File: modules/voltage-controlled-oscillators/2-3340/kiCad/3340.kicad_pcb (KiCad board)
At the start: 2 copper layers, 21 parts, among them J1 PWR, J2 INPUT, J3 OUTPUT

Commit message: cleaning up the main readme, update for 3340-vco
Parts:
- removed C1, C2: 47uF, Capacitor_THT:CP_Radial_D6.3mm_P2.50mm
- removed C3: 0.1uF, Capacitor_THT:CP_Radial_D4.0mm_P2.00mm
- removed the C5 at (108.2, 67.0)
- removed the C5 at (97.8, 71.2)
- removed the C6 at (94.7, 80.9)
- removed the C6 at (87.5, 80.5)
- added C10: 47uF, Capacitor_THT:CP_Radial_D6.3mm_P2.50mm, F.Cu at (34.4, 50.0)
- added C11: 0.1uF, Capacitor_THT:CP_Radial_D4.0mm_P2.00mm, F.Cu at (41.7, 42.1)
- added C12: 0.1uF, Capacitor_THT:CP_Radial_D4.0mm_P2.00mm, F.Cu at (41.7, 47.7)
- added C5: 0.1uF, Capacitor_THT:CP_Radial_D4.0mm_P2.00mm, F.Cu at (95.4, 94.5)
- added C6: 0.1uF, Capacitor_THT:CP_Radial_D4.0mm_P2.00mm, F.Cu at (95.4, 100.0)
- added C7: 0.1uF, Capacitor_THT:CP_Radial_D4.0mm_P2.00mm, F.Cu at (95.4, 105.5)
- added C9: 47uF, Capacitor_THT:CP_Radial_D6.3mm_P2.50mm, F.Cu at (34.4, 42.1)
- added J10: 1V/OCT, Synth:Jack_3.5mm_QingPu_WQP-PJ398SM_Vertical_CircularHoles, F.Cu at (226.2, 23.8)
- added J4: PWR, Synth:IDC-Header_2x08_P2.54mm_Vertical, B.Cu at (54.9, 65.3)
- added J5: SQR, Synth:Jack_3.5mm_QingPu_WQP-PJ398SM_Vertical_CircularHoles, F.Cu at (182.7, 23.9)
- added J6: TRI, Synth:Jack_3.5mm_QingPu_WQP-PJ398SM_Vertical_CircularHoles, F.Cu at (193.7, 23.9)
- added J7: SAW, Synth:Jack_3.5mm_QingPu_WQP-PJ398SM_Vertical_CircularHoles, F.Cu at (204.8, 23.9)
- added J8: SIN, Synth:Jack_3.5mm_QingPu_WQP-PJ398SM_Vertical_CircularHoles, F.Cu at (215.8, 23.9)
- added J9: PWM, Synth:Jack_3.5mm_QingPu_WQP-PJ398SM_Vertical_CircularHoles, F.Cu at (237.0, 23.6)
- added Q1: 2N3904, Package_TO_SOT_THT:TO-92L_HandSolder, F.Cu at (153.6, 77.2)
- added Q2: 2N3904, Package_TO_SOT_THT:TO-92L_HandSolder, F.Cu at (153.6, 83.3)
- added R10: 10M (OPT), Synth:R_Default (DIN0207), F.Cu at (116.5, 68.8)
- added R11: 100K, Synth:R_Default (DIN0207), F.Cu at (116.5, 72.9)
- added R12: 100K, Synth:R_Default (DIN0207), F.Cu at (116.5, 77.0)
- added R13: 100K, Synth:R_Default (DIN0207), F.Cu at (116.5, 81.0)
- added R14: 10K, 1%, Synth:R_Default (DIN0207), F.Cu at (116.5, 85.0)
- added R15: 10K, 1%, Synth:R_Default (DIN0207), F.Cu at (116.5, 89.1)
- added R16: 1K, Synth:R_Default (DIN0207), F.Cu at (116.5, 93.2)
- added R17: 1K, Synth:R_Default (DIN0207), F.Cu at (116.5, 97.2)
- added R18: 1K, Synth:R_Default (DIN0207), F.Cu at (116.5, 101.2)
- added R19: 1K, Synth:R_Default (DIN0207), F.Cu at (116.5, 105.3)
- added R20: 100K, Potentiometer_THT:Potentiometer_Bourns_3296W_Vertical, F.Cu at (159.7, 57.5)
- added R21: 2.2K, 1%, Synth:R_Default (DIN0207), F.Cu at (130.6, 58.2)
- added R22: 10K, 1%, Synth:R_Default (DIN0207), F.Cu at (130.6, 62.2)
- added R23: 390R, Synth:R_Default (DIN0207), F.Cu at (130.6, 66.3)
- added R24: 50K, Potentiometer_THT:Potentiometer_Bourns_3296W_Vertical, F.Cu at (159.7, 64.0)
- added R25: 18K, Synth:R_Default (DIN0207), F.Cu at (130.6, 70.3)
- added R26: 10K, 1%, Synth:R_Default (DIN0207), F.Cu at (130.6, 74.4)
- added R27: 2.2K, 1%, Synth:R_Default (DIN0207), F.Cu at (130.6, 78.5)
- added R28: 20K, 1%, Synth:R_Default (DIN0207), F.Cu at (130.6, 82.5)
- added R29: 5K, Potentiometer_THT:Potentiometer_Bourns_3296W_Vertical, F.Cu at (159.7, 70.4)
- added R3: 470, Synth:R_Default (DIN0207), F.Cu at (116.5, 40.5)
- added R30: 20K, 1%, Synth:R_Default (DIN0207), F.Cu at (130.6, 86.5)
- added R31: 1K, Synth:R_Default (DIN0207), F.Cu at (130.6, 31.9)
- added R32: 470K, Synth:R_Default (DIN0207), F.Cu at (130.6, 36.0)
- added R33: 470K, Synth:R_Default (DIN0207), F.Cu at (130.6, 40.0)
- added R34: 470K, Synth:R_Default (DIN0207), F.Cu at (130.6, 44.0)
- added R35: 100K, Synth:R_Default (DIN0207), F.Cu at (130.6, 48.1)
- added R36: 4K7, Synth:R_Default (DIN0207), F.Cu at (130.6, 52.1)
- added R37: 100K, Synth:R_Default (DIN0207), F.Cu at (130.2, 90.8)
- added R38: 220K, Synth:R_Default (DIN0207), F.Cu at (130.2, 94.8)
- added R39: 100K, Synth:R_Default (DIN0207), F.Cu at (130.2, 98.8)
- added R4: 24K, Synth:R_Default (DIN0207), F.Cu at (116.5, 44.5)
- added R40: 1M, Synth:R_Default (DIN0207), F.Cu at (130.2, 102.9)
- added R41: 360K, Synth:R_Default (DIN0207), F.Cu at (130.2, 107.0)
- added R42: 100K, Synth:R_Default (DIN0207), F.Cu at (130.2, 111.0)
- added R43: 470, Synth:R_Default (DIN0207), F.Cu at (130.2, 115.0)
- added R44: 1M, Synth:R_Default (DIN0207), F.Cu at (130.2, 119.1)
- added R5: 5.6K, Synth:R_Default (DIN0207), F.Cu at (116.5, 48.6)
- added R6: 1.8K, Synth:R_Default (DIN0207), F.Cu at (116.5, 52.6)
- added R7: 10, Synth:R_Default (DIN0207), F.Cu at (116.5, 56.7)
- added R8: 10, Synth:R_Default (DIN0207), F.Cu at (116.5, 60.8)
- added R9: 820, Synth:R_Default (DIN0207), F.Cu at (116.5, 64.8)
- added RV2: B100K, Synth:Potentiometer_Alpha_RD901F-40-00D_Single_Vertical_CircularHoles, F.Cu at (206.1, 102.4)
- added RV3: B100K, Synth:Potentiometer_Alpha_RD901F-40-00D_Single_Vertical_CircularHoles, F.Cu at (220.5, 102.4)
- added SW1: HARD/SOFT, Synth:SW_default, F.Cu at (225.1, 44.1)
- added U1: TL074, Package_DIP:DIP-14_W7.62mm_Socket_LongPads, F.Cu at (73.2, 73.4)
- added U2: TL074, Package_DIP:DIP-14_W7.62mm_Socket_LongPads, F.Cu at (85.0, 73.4)
- added U3: CEM3340, Package_DIP:DIP-16_W7.62mm_Socket_LongPads, F.Cu at (84.2, 92.9)
- added course1: B100K, Synth:Potentiometer_TT_P0915N, F.Cu at (237.0, 85.5)
- added fine1: B100K, Synth:Potentiometer_TT_P0915N, F.Cu at (237.0, 100.3)
- D1, D2: footprint Diode_THT:D_DO-41_SOD81_P10.16mm_Horizontal -> Synth:D_DO-41_SOD81_P10.16mm_Horizontal
- H1: value TOP_4_SGL -> TOP_8_SGL; footprint synth-custom:PinHeader_1x04_P2.00mm_Vertical -> Synth:PinHeader_1x08_P2.54mm_Vertical
- H2: value BTM_4_SGL -> BTM_8_SGL; footprint synth-custom:PinSocket_1x04_P2.00mm_Vertical -> Synth:PinSocket_1x08_P2.54mm_Vertical
- H3: value TOP_8_SGL -> TOP_4_SGL; footprint synth-custom:PinHeader_1x08_P2.00mm_Vertical -> Synth:PinHeader_1x04_P2.54mm_Vertical
- H4: value BTM_8_SGL -> BTM_4_SGL; footprint synth-custom:PinSocket_1x08_P2.00mm_Vertical -> Synth:PinSocket_1x04_P2.54mm_Vertical
- H5: footprint synth-custom:PinHeader_1x08_P2.00mm_Vertical -> Synth:PinHeader_1x08_P2.54mm_Vertical
- H6: footprint synth-custom:PinSocket_1x08_P2.00mm_Vertical -> Synth:PinSocket_1x08_P2.54mm_Vertical
- J1: value PWR -> FM; footprint synth-custom:CONN_02x08_PWR -> Synth:Jack_3.5mm_QingPu_WQP-PJ398SM_Vertical_CircularHoles
- J2: value INPUT -> SYNC; footprint synth-custom:Jack_3.5mm_QingPu_WQP-PJ398SM_Vertical_CircularHoles -> Synth:Jack_3.5mm_QingPu_WQP-PJ398SM_Vertical_CircularHoles
- J3: value OUTPUT -> CV_INPUT; footprint synth-custom:Jack_3.5mm_QingPu_WQP-PJ398SM_Vertical_CircularHoles -> Connector_PinHeader_2.54mm:PinHeader_1x03_P2.54mm_Vertical
- R1: value 10 -> 1.5M; footprint synth-custom:R_Axial_DIN0207_L6.3mm_D2.5mm_P7.62mm_Horizontal -> Synth:R_Default (DIN0207)
- R2: value 10 -> 1M; footprint synth-custom:R_Axial_DIN0207_L6.3mm_D2.5mm_P7.62mm_Horizontal -> Synth:R_Default (DIN0207)
- moved H1 102.3 mm to (17.9, 134.5)
- moved J1 102.2 mm to (160.6, 23.9)
- moved H2 98.7 mm to (27.2, 134.5)
- moved J2 98.7 mm to (171.6, 23.9)
- moved H5 94.0 mm to (22.6, 134.5)
- moved H6 90.9 mm to (31.8, 134.5)
- moved H3 90.5 mm to (37.3, 143.6)
- moved H4 90.3 mm to (42.0, 143.6)
- moved R1 71.2 mm to (116.5, 32.4)
- moved R2 71.2 mm to (116.5, 36.5)
- moved D1 44.6 mm to (29.8, 62.0)
- moved D2 44.6 mm to (29.8, 66.2)
- moved C4 30.3 mm to (95.4, 88.9)
- moved J3 22.6 mm to (63.5, 44.0)
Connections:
- C4 pad 1: GNDREF -> +12V
- C4 pad 2: -12V -> GNDREF
- J2 pad S: unconnected-(J2-PadS) -> GNDREF
- J2 pad T: unconnected-(J2-PadT) -> Net-(C1-Pad1)
- J2 pad TN: unconnected-(J2-PadTN) -> GNDREF
- R1 pad 2: +12V -> /LIN_FM
- R2 pad 1: -12V -> Net-(C2-Pad2)
- R2 pad 2: -12V -> /LIN_FM

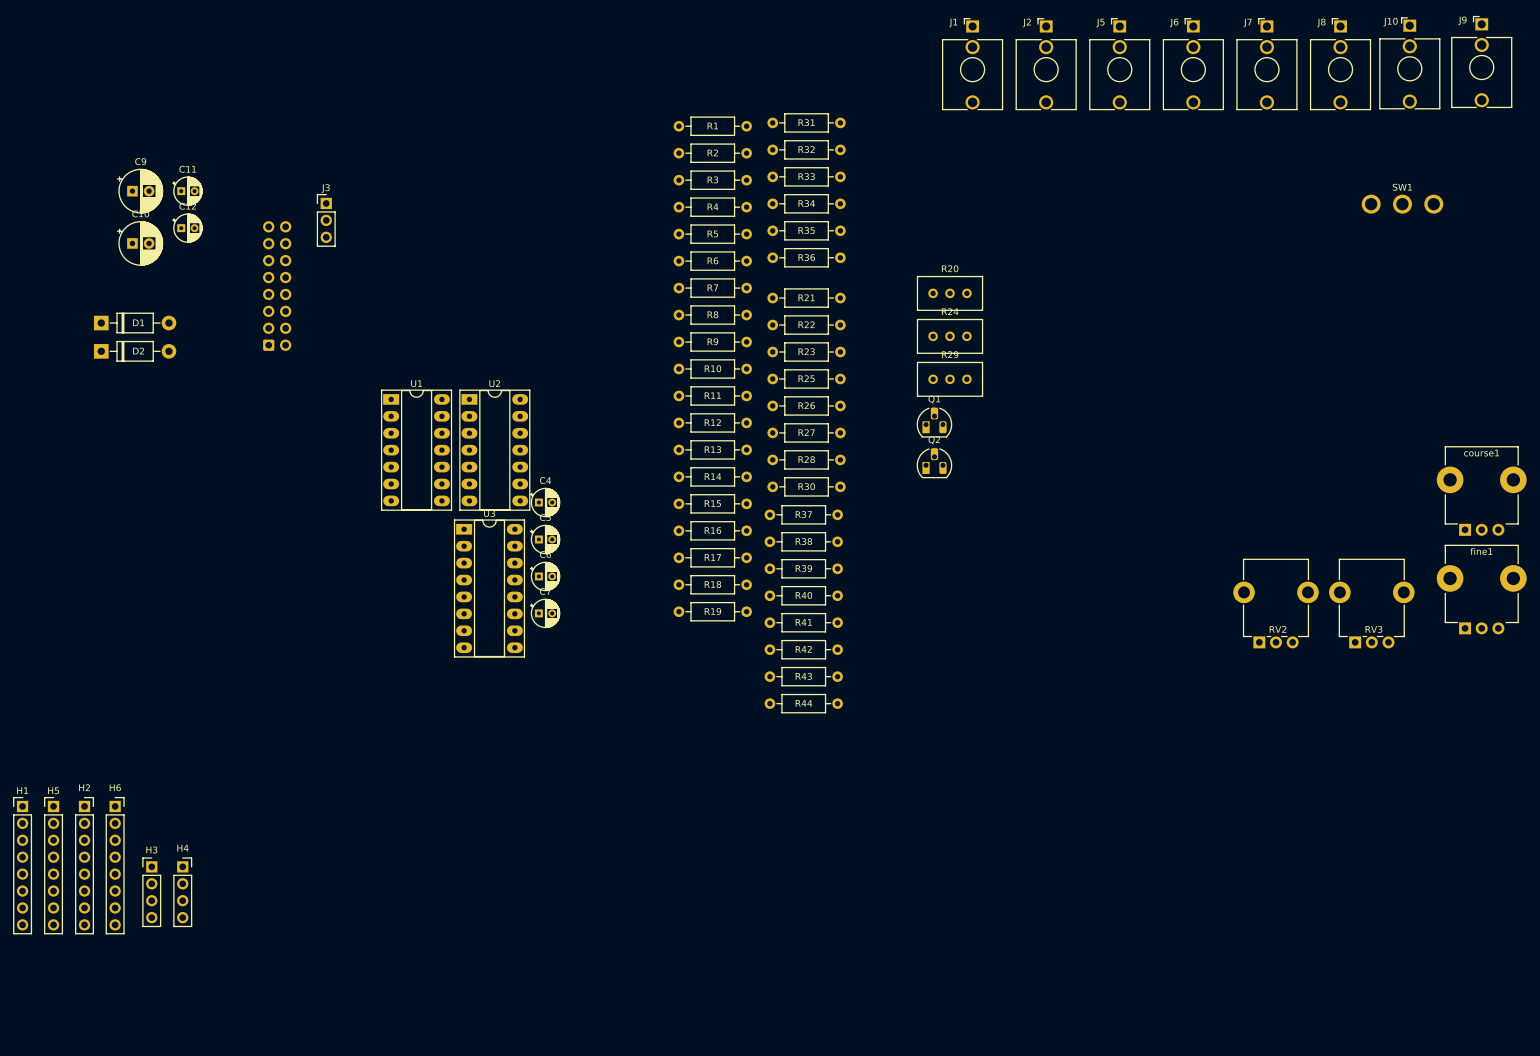
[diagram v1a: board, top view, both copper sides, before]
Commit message: updated 3340, LFO and 7555 schematics and PCB
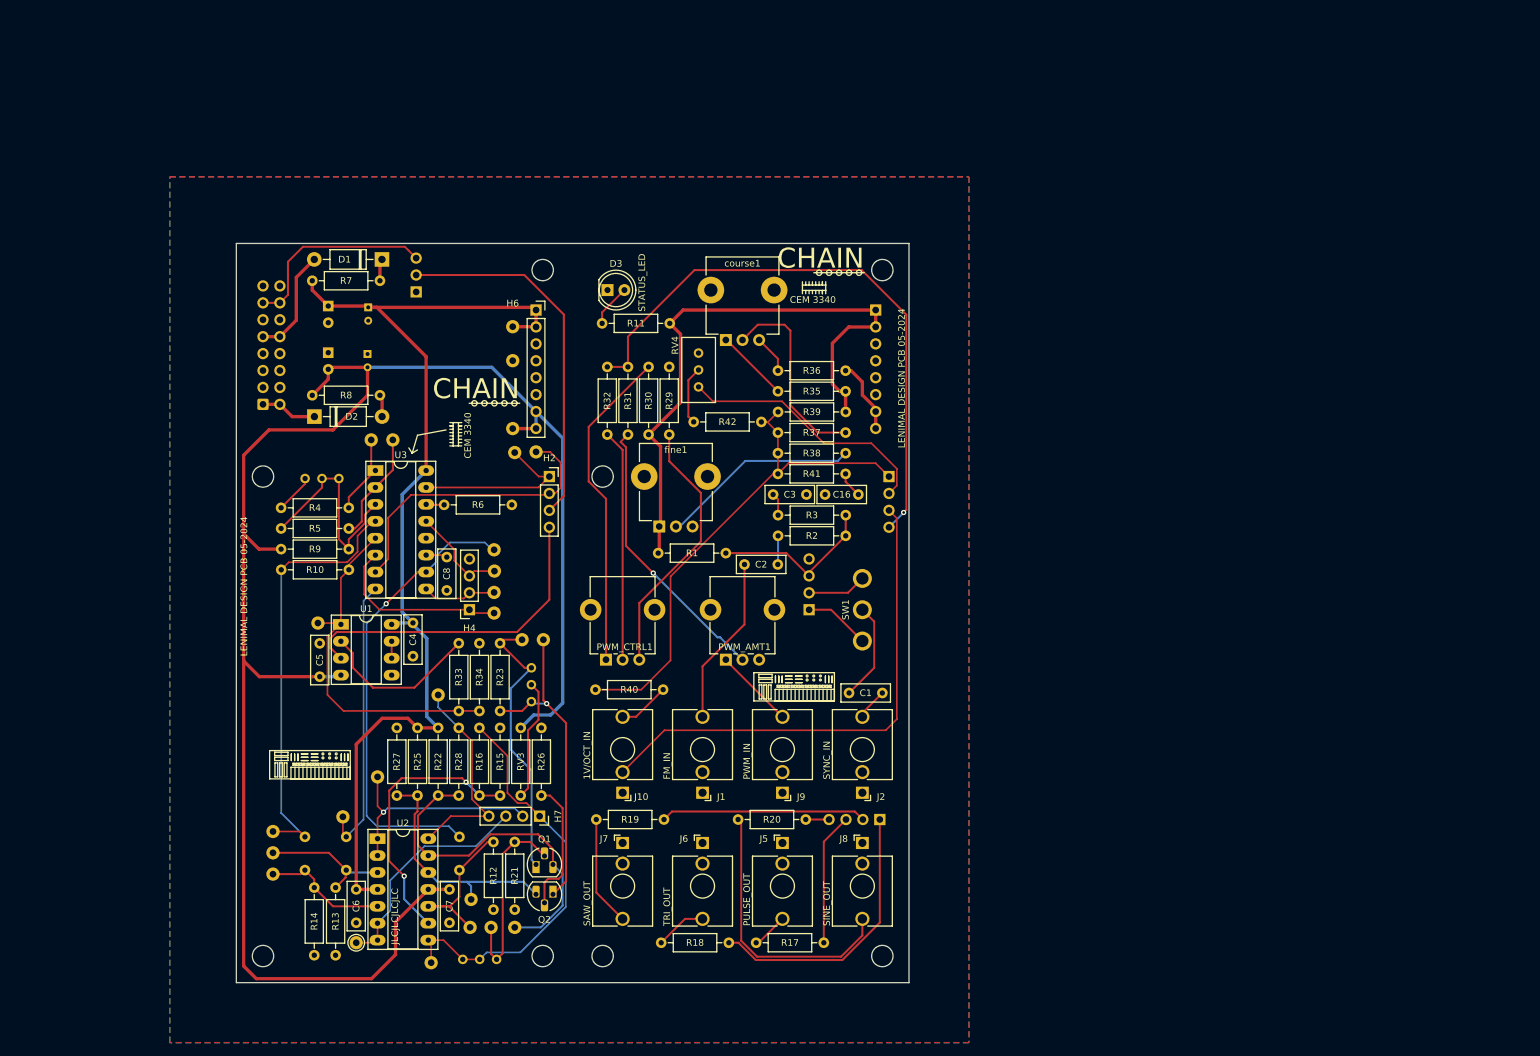
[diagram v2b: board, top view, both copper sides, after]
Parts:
- removed R43: 470, Synth:R_Default (DIN0207)
- removed R44: 1M, Synth:R_Default (DIN0207)
- added C1: 0.001uF, Synth:C_RECT_WIMA_0.1uF, F.Cu at (147.0, 117.5)
- added C13: 1 uF, Synth:C_RECT_MKT_1uF, B.Cu at (60.3, 139.1)
- added C14: 1 uF, Synth:C_RECT_MKT_1uF, B.Cu at (66.5, 139.1)
- added C15: 1 uF, Synth:C_RECT_MKT_1uF, B.Cu at (83.5, 139.1)
- added C16: 0.1uF, Synth:C_RECT_WIMA_0.1uF, F.Cu at (143.4, 87.7)
- added C2: 0.1uF, Synth:C_RECT_WIMA_0.1uF, F.Cu at (126.3, 98.2)
- added C3: 0.01 uF, Synth:C_RECT_WIMA_0.1uF, F.Cu at (130.6, 87.7)
- added C8: 1nF, Synth:C_RECT_WIMA_0.1uF, F.Cu at (81.6, 102.1)
- added D3: LED, Synth:LED_D5.0mm (center Aligned), F.Cu at (107.0, 57.0)
- added H10: MountingHole, MountingHole:MountingHole_3.2mm_M3, F.Cu at (96.0, 54.0)
- added H11: MountingHole, MountingHole:MountingHole_3.2mm_M3, F.Cu at (54.0, 85.0)
- added H12: MountingHole, MountingHole:MountingHole_3.2mm_M3, F.Cu at (105.0, 85.0)
- added H13: MountingHole, MountingHole:MountingHole_3.2mm_M3, F.Cu at (54.0, 157.0)
- added H14: MountingHole, MountingHole:MountingHole_3.2mm_M3, F.Cu at (147.0, 157.0)
- added H15: MountingHole, MountingHole:MountingHole_3.2mm_M3, F.Cu at (105.0, 157.0)
- added H16: MountingHole, MountingHole:MountingHole_3.2mm_M3, F.Cu at (96.0, 157.0)
- added H7: BTM_4_SGL, Synth:PinSocket_1x04_P2.54mm_Vertical, F.Cu at (95.5, 136.0)
- added H8: TOP_4_SGL, Synth:PinHeader_1x04_P2.54mm_Vertical, B.Cu at (146.6, 136.5)
- added H9: MountingHole, MountingHole:MountingHole_3.2mm_M3, F.Cu at (147.0, 54.0)
- added PWM_AMT1: B100K, Synth:Potentiometer_Alpha_RD901F-40-00D_Single_Vertical_CircularHoles, F.Cu at (126.0, 105.0)
- added PWM_CTRL1: B100K, Synth:Potentiometer_Alpha_RD901F-40-00D_Single_Vertical_CircularHoles, F.Cu at (108.0, 105.0)
- added RV1: 10K, Potentiometer_THT:Potentiometer_Bourns_3296W_Vertical, B.Cu at (60.3, 85.3)
- added RV4: 20K, Potentiometer_THT:Potentiometer_Bourns_3296W_Vertical, F.Cu at (119.4, 66.5)
- added TP1: SOFT_SYNC, Connector_Pin:Pin_D1.0mm_L10.0mm, B.Cu at (88.7, 102.4)
- added TP10: -12V, Connector_Pin:Pin_D1.0mm_L10.0mm, B.Cu at (91.5, 77.8)
- added TP11: GNDREF, Connector_Pin:Pin_D1.0mm_L10.0mm, B.Cu at (91.5, 67.6)
- added TP12: PULSE_RAW, Connector_Pin:Pin_D1.0mm_L10.0mm, B.Cu at (55.5, 138.3)
- added TP13: SAW_RAW, Connector_Pin:Pin_D1.0mm_L10.0mm, B.Cu at (66.0, 136.1)
- added TP14: TRI_RAW, Connector_Pin:Pin_D1.0mm_L10.0mm, B.Cu at (88.7, 96.0)
- added TP15: PULSE_IN, Connector_Pin:Pin_D1.0mm_L10.0mm, B.Cu at (55.5, 144.7)
- added TP16: SAW_IN, Connector_Pin:Pin_D1.0mm_L10.0mm, B.Cu at (55.5, 141.5)
- added TP17: TRI_IN, Connector_Pin:Pin_D1.0mm_L10.0mm, B.Cu at (85.1, 152.7)
- added TP18: PULSE_OUT, Connector_Pin:Pin_D1.0mm_L10.0mm, F.Cu at (68.0, 155.0)
- added TP19: SAW_OUT, Connector_Pin:Pin_D1.0mm_L10.0mm, B.Cu at (71.2, 130.1)
- added TP2: HI_FREQ_TRACK, Connector_Pin:Pin_D1.0mm_L10.0mm, B.Cu at (95.0, 81.3)
- added TP20: TRI_OUT, Connector_Pin:Pin_D1.0mm_L10.0mm, B.Cu at (79.2, 158.0)
- added TP21: SIN_OUT, Connector_Pin:Pin_D1.0mm_L10.0mm, B.Cu at (80.3, 117.8)
- added TP22: SIN_IN, Connector_Pin:Pin_D1.0mm_L10.0mm, B.Cu at (88.2, 152.7)
- added TP23: SIN_Q1, Connector_Pin:Pin_D1.0mm_L10.0mm, B.Cu at (92.9, 109.5)
- added TP24: SIN_Q2, Connector_Pin:Pin_D1.0mm_L10.0mm, B.Cu at (96.1, 109.5)
- added TP25: SIN_NON_INVERTED, Connector_Pin:Pin_D1.0mm_L10.0mm, B.Cu at (85.2, 148.5)
- added TP26: SIN_INVERTED, Connector_Pin:Pin_D1.0mm_L10.0mm, B.Cu at (91.8, 152.7)
- added TP3: HARD_SYNC, Connector_Pin:Pin_D1.0mm_L10.0mm, B.Cu at (88.7, 105.5)
- added TP4: VPWM, Connector_Pin:Pin_D1.0mm_L10.0mm, B.Cu at (62.2, 107.0)
- added TP5: LIN_FREQ, Connector_Pin:Pin_D1.0mm_L10.0mm, B.Cu at (88.8, 99.2)
- added TP6: FREQ, Connector_Pin:Pin_D1.0mm_L10.0mm, B.Cu at (91.8, 81.4)
- added TP7: SCALE_1, Connector_Pin:Pin_D1.0mm_L10.0mm, B.Cu at (70.2, 79.5)
- added TP8: SCALE_2, Connector_Pin:Pin_D1.0mm_L10.0mm, B.Cu at (73.5, 79.5)
- added TP9: +12V, Connector_Pin:Pin_D1.0mm_L10.0mm, B.Cu at (91.5, 62.5)
- C10, C11, C12, C9, H3, H5, J3, R24: moved to B.Cu
- C4, C5, C6, C7: footprint Capacitor_THT:CP_Radial_D4.0mm_P2.00mm -> Synth:C_RECT_WIMA_0.1uF
- H1: value TOP_8_SGL -> TOP_4_SGL; footprint Synth:PinHeader_1x08_P2.54mm_Vertical -> Synth:PinHeader_1x04_P2.54mm_Vertical; moved to B.Cu
- H2: value BTM_8_SGL -> BTM_4_SGL; footprint Synth:PinSocket_1x08_P2.54mm_Vertical -> Synth:PinSocket_1x04_P2.54mm_Vertical
- R11: value 100K -> 470R
- R14: value 10K, 1% -> 100K
- R16: value 1K -> 10K, 1%
- R20: value 100K -> 1K; footprint Potentiometer_THT:Potentiometer_Bourns_3296W_Vertical -> Synth:R_Default (DIN0207)
- R25: value 18K -> 10K, 1%
- R26: value 10K, 1% -> 2.2K, 1%
- R27: value 2.2K, 1% -> 10K, 1%
- R28: value 20K, 1% -> 10K, 1%
- R29: value 5K -> 1K; footprint Potentiometer_THT:Potentiometer_Bourns_3296W_Vertical -> Synth:R_Default (DIN0207)
- R30: value 20K, 1% -> 470K
- R31: value 1K -> 470K
- R33: value 470K -> 100K
- R34: value 470K -> 4K7
- R36: value 4K7 -> 220K
- R38: value 220K -> 1M
- R39: value 100K -> 200K - 360K
- R40: value 1M -> 100K
- R41: value 360K -> 470
- R42: value 100K -> 1M
- RV2: value B100K -> 100K; footprint Synth:Potentiometer_Alpha_RD901F-40-00D_Single_Vertical_CircularHoles -> Potentiometer_THT:Potentiometer_Bourns_3296W_Vertical; moved to B.Cu
- RV3: value B100K -> 18K; footprint Synth:Potentiometer_Alpha_RD901F-40-00D_Single_Vertical_CircularHoles -> Synth:R_Default (DIN0207)
- U1: value TL074 -> TL072; footprint Package_DIP:DIP-14_W7.62mm_Socket_LongPads -> Package_DIP:DIP-8_W7.62mm_Socket_LongPads
- moved J10 156.3 mm to (108.0, 126.0), turned to 180 degrees
- moved J7 156.2 mm to (108.0, 146.5)
- moved J9 146.7 mm to (132.0, 126.0), turned to 180 degrees
- moved H5 144.2 mm to (146.0, 60.0), turned to 180 degrees
- moved J6 143.0 mm to (120.0, 146.5)
- moved J8 142.1 mm to (144.0, 146.5)
- moved H1 139.2 mm to (148.0, 85.0), turned to 180 degrees
- moved RV2 134.0 mm to (84.0, 157.5), turned to 180 degrees
- moved J5 132.7 mm to (132.0, 146.5)
- moved RV3 129.4 mm to (92.7, 122.8), turned to -90 degrees
- moved fine1 122.0 mm to (116.0, 85.0)
- moved course1 114.6 mm to (126.0, 57.0)
- moved J1 109.9 mm to (120.0, 126.0), turned to 180 degrees
- moved H3 106.0 mm to (136.0, 105.0)
- moved J2 105.8 mm to (144.0, 126.0), turned to 180 degrees
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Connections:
- D1 pad 1: +12V -> Net-(D1-K)
- D1 pad 2: +12V -> Net-(D1-A)
- D2 pad 1: -12V -> Net-(D2-K)
- D2 pad 2: -12V -> Net-(D2-A)
- H1 pad 1: unconnected-(H1A-Pin_1-Pad1) -> /cv_input/FREQ
- H1 pad 2: unconnected-(H1B-Pin_2-Pad2) -> /cv_input/HIGH_FREQ_TRACKING
- H1 pad 3: unconnected-(H1C-Pin_3-Pad3) -> /cv_input/CV_INPUT
- H1 pad 4: unconnected-(H1D-Pin_4-Pad4) -> Net-(H1D-Pin_4)
- H2 pad 1: unconnected-(H2A-Pin_3-Pad1) -> /FREQ
- H2 pad 2: unconnected-(H2B-Pin_2-Pad2) -> /HI_FREQ_TRACK
- H2 pad 3: unconnected-(H2C-Pin_3-Pad3) -> Net-(H2C-Pin_3)
- H2 pad 4: unconnected-(H2D-Pin_4-Pad4) -> Net-(H2D-Pin_4)
- H3 pad 1: unconnected-(H3A-Pin_1-Pad1) -> Net-(H3A-Pin_1)
- H3 pad 2: unconnected-(H3B-Pin_2-Pad2) -> Net-(H3B-Pin_2)
- H3 pad 3: unconnected-(H3C-Pin_3-Pad3) -> Net-(H3C-Pin_3)
- H3 pad 4: unconnected-(H3D-Pin_4-Pad4) -> GNDREF
- H4 pad 1: unconnected-(H4A-Pin_1-Pad1) -> /HARD SYNC
- H4 pad 2: unconnected-(H4B-Pin_2-Pad2) -> /SOFT SYNC
- H4 pad 3: unconnected-(H4C-Pin_3-Pad3) -> /LIN_FM
- H4 pad 4: unconnected-(H4D-Pin_4-Pad4) -> GNDREF
- H5 pad 2: unconnected-(H5B-Pin_2-Pad2) -> +12V
- H5 pad 3: unconnected-(H5C-Pin_3-Pad3) -> GNDREF
- H5 pad 6: unconnected-(H5F-Pin_6-Pad6) -> GNDREF
- H5 pad 7: unconnected-(H5G-Pin_7-Pad7) -> -12V
- H6 pad 2: unconnected-(H6B-Pin_2-Pad2) -> +12V
- H6 pad 3: unconnected-(H6C-Pin_3-Pad3) -> GNDREF
- H6 pad 6: unconnected-(H6F-Pin_6-Pad6) -> GNDREF
- H6 pad 7: unconnected-(H6G-Pin_7-Pad7) -> -12V
- J3 pad 2: /cv_input/CV_INPUT -> Net-(H2C-Pin_3)
- J4 pad 1: -12V -> Net-(D2-K)
- J4 pad 10: +12V -> Net-(D1-A)
- J4 pad 2: -12V -> Net-(D2-K)
- J4 pad 9: +12V -> Net-(D1-A)
- R1 pad 2: /LIN_FM -> Net-(H3C-Pin_3)
- R11 pad 1: GNDREF -> +12V
- R11 pad 2: Net-(U2C-+) -> Net-(D3-A)
- R12 pad 2: Net-(U2A-+) -> Net-(U2C-+)
- R13 pad 2: Net-(U2B-+) -> Net-(U2A-+)
- R14 pad 1: Net-(U2C--) -> GNDREF
- R14 pad 2: GNDREF -> Net-(U2B-+)
- R15 pad 1: /TRI +-5V PP -> Net-(U2C--)
- R15 pad 2: Net-(U2C--) -> GNDREF
- R16 pad 1: /PULSE +-5V PP -> /TRI +-5V PP
- R16 pad 2: Net-(J5-PadT) -> Net-(U2C--)
- R17 pad 1: /TRI +-5V PP -> Net-(H8C-Pin_3)
- R17 pad 2: Net-(J6-PadT) -> Net-(J5-PadT)
- R18 pad 1: /SAW +-5V PP -> Net-(H8A-Pin_1)
- R18 pad 2: Net-(J7-PadT) -> Net-(J6-PadT)
- R19 pad 1: Net-(J8-PadT) -> Net-(H8B-Pin_2)
- R19 pad 2: /SINE +-5V PP -> Net-(J7-PadT)
- R2 pad 2: /LIN_FM -> Net-(H3C-Pin_3)
- R20 pad 1: /TRI +-5V PP -> Net-(J8-PadT)
- R20 pad 2: /TRI +-5V PP -> Net-(H8D-Pin_4)
- R25 pad 1: -12V -> Net-(Q2-C)
- R25 pad 2: Net-(R24-Pad2) -> +12V
- R26 pad 1: Net-(Q2-C) -> Net-(Q2-B)
- R26 pad 2: +12V -> GNDREF
- R27 pad 1: Net-(Q2-B) -> GNDREF
- R27 pad 2: GNDREF -> Net-(Q2-C)
- R28 pad 1: GNDREF -> /SINE +-5V PP
- R28 pad 2: Net-(Q2-C) -> Net-(Q1-C)
- R29 pad 1: Net-(Q1-C) -> GNDREF
- R29 pad 2: GNDREF -> Net-(PWM_CTRL1-Pad3)
- R3 pad 2: /LIN_FM -> Net-(H3C-Pin_3)
- R30 pad 1: /SINE +-5V PP -> Net-(PWM_CTRL1-Pad1)
- R30 pad 2: Net-(Q1-C) -> +12V
- R31 pad 1: GNDREF -> Net-(H1D-Pin_4)
- R31 pad 2: Net-(R31-Pad2) -> Net-(PWM_AMT1-Pad2)
- R32 pad 1: Net-(R32-Pad1) -> Net-(H1D-Pin_4)
- R32 pad 2: +12V -> Net-(PWM_CTRL1-Pad2)
- R33 pad 1: Net-(U1A-+) -> /VPWM
- R33 pad 2: Net-(R33-Pad2) -> Net-(U1A--)
- R34 pad 1: Net-(U1A-+) -> GNDREF
- R34 pad 2: Net-(R34-Pad2) -> /VPWM
- R35 pad 1: /VPWM -> +12V
- R35 pad 2: Net-(U1A--) -> Net-(R35-Pad2)
- R36 pad 1: GNDREF -> Net-(R36-Pad1)
- R36 pad 2: /VPWM -> -12V
- R37 pad 1: +12V -> /cv_input/FREQ
- R38 pad 1: Net-(R38-Pad1) -> /cv_input/FREQ
- R38 pad 2: -12V -> Net-(R38-Pad2)
- R39 pad 1: /FREQ -> /cv_input/FREQ
- R39 pad 2: Net-(R39-Pad2) -> +12V
- R40 pad 1: /FREQ -> /cv_input/FREQ
- R40 pad 2: Net-(R40-Pad2) -> Net-(J10-PadT)
- R41 pad 1: /FREQ -> /cv_input/FREQ
- R41 pad 2: +12V -> Net-(C16-Pad1)
- R42 pad 1: /FREQ -> /cv_input/FREQ
- R42 pad 2: Net-(J10-PadT) -> Net-(R42-Pad2)
- R7 pad 2: +12V -> Net-(D1-K)
- R8 pad 2: -12V -> Net-(D2-A)
- RV2 pad 1: Net-(J9-PadT) -> /TRI +-5V PP
- RV2 pad 2: Net-(R33-Pad2) -> /TRI +-5V PP
- RV2 pad 3: GNDREF -> Net-(Q1-B)
- RV3 pad 1: Net-(R32-Pad1) -> -12V
- RV3 pad 2: Net-(R34-Pad2) -> Net-(R24-Pad2)
- SW1 pad 1: /HARD SYNC -> Net-(H3A-Pin_1)
- SW1 pad 3: /SOFT SYNC -> Net-(H3B-Pin_2)
- U1 pad 3: Net-(U1A-+) -> Net-(H2D-Pin_4)
- U1 pad 4: +12V -> -12V
- U1 pad 8: Net-(U1C--) -> +12V
- course1 pad 1: Net-(R37-Pad2) -> Net-(R35-Pad2)
- course1 pad 2: Net-(R39-Pad2) -> Net-(R37-Pad2)
- course1 pad 3: Net-(R38-Pad1) -> Net-(R36-Pad1)
- fine1 pad 2: Net-(R40-Pad2) -> Net-(R38-Pad2)
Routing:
- net -12V: track 0.00 -> 274.9 mm
- net +12V: track 0.00 -> 247.8 mm
- net Net-(H1D-Pin_4): track 0.00 -> 89.4 mm, vias 0 -> 1
- net /cv_input/FREQ: track 0.00 -> 78.9 mm
- net /cv_input/CV_INPUT: track 0.00 -> 76.3 mm
- net /TRI 0-5V PP: track 0.00 -> 69.3 mm, vias 0 -> 1
- net /PULSE 0-12V PP: track 0.00 -> 65.3 mm
- net /TRI +-5V PP: track 0.00 -> 61.7 mm
- net Net-(H2C-Pin_3): track 0.00 -> 54.9 mm
- net /VPWM: track 0.00 -> 54.0 mm
- net Net-(Q1-C): track 0.00 -> 52.6 mm
- net Net-(H2D-Pin_4): track 0.00 -> 49.8 mm
- net Net-(PWM_CTRL1-Pad1): track 0.00 -> 48.8 mm
- net Net-(Q2-E): track 0.00 -> 48.2 mm, vias 0 -> 1
- net /HI_FREQ_TRACK: track 0.00 -> 44.9 mm
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- added copper zone on F.Cu, net (none)
- added copper zone on B.Cu, net GNDREF
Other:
- board outline added: 101 x 111 mm
- board text added: "+12V"
- board text added: "-12V"
- board text added: "0"
- board text added: "1"
- board text added: "1V/OCT_IN"
- board text added: "CEM 3340"
- board text added: "CHAIN"
- board text added: "CV FROM BUS"
- board text added: "FM_IN"
- board text added: "FREQ"
- board text added: "GND"
- board text added: "HARD_SYNC"
- board text added: "HI_TRACK"
- board text added: "JLCJLCJLCJLC"
- board text added: "LENIMAL DESIGN PCB 05-2024"
- board text added: "LIN_FREQ"
- board text added: "PULSE_IN"
- board text added: "PULSE_OUT"
- board text added: "PULSE_SAW"
- board text added: "PWM"
- board text added: "PWM_IN"
- board text added: "Q1"
- board text added: "Q2"
- board text added: "SAW_IN"
- board text added: "SAW_OUT"
- board text added: "SAW_RAW"
- board text added: "SCALE 1 2"
- board text added: "SINE_OUT"
- board text added: "SIN_INT"
- board text added: "SIN_INV"
- board text added: "SIN_N-INV"
- board text added: "SIN_OUT"
- board text added: "SOFT_SYNC"
- board text added: "STATUS_LED"
- board text added: "SYNC_IN"
- board text added: "TRI_IN"
- board text added: "TRI_OUT"
- board text added: "TRI_RAW"
- board text added: "This module is based around the CEM 3340. When I saw the datasheet, I was afraid of trying it out. But thanks to the internet I managed to get this module working!"
- board text added: "v1"

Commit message: update components, PCB 3320 and design
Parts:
- added G***: LOGO, Synth:lenimal_logo_full, F.Cu at (126.5, 158.5)
- added G***: LOGO, Synth:lenimal_logo_full, B.Cu at (67.5, 159.5)
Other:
- board text added: "REV.1"

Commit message: update component status, add IBOM for built modules
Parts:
- H1, H3, H8: value TOP_4_SGL -> ~
- H2, H4, H7: value BTM_4_SGL -> ~
- H5: value TOP_8_PWR -> ~
- H6: value BTM_8_PWR -> ~
- R1: value 1.5M -> 1M5
- R10: value 10M (OPT) -> 10M [optional]
- R15, R16, R22, R25, R27, R28: value 10K, 1% -> 10K [1%]
- R21, R26: value 2.2K, 1% -> 2K2 [1%]
- R3, R41: value 470 -> 470R
- R39: value 200K - 360K -> 220K
- R5: value 5.6K -> 5K6
- R6: value 1.8K -> 1K8
- R7, R8: value 10 -> 10R
- R9: value 820 -> 820R
